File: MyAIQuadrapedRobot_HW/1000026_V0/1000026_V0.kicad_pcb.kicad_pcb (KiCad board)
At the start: 4 copper layers, 100 x 70 mm, 27 parts, among them J1 533750410, J2 0525591853, J3 532580229, J5 532580229, J9 0525591853, SW1 TL3305CF260QG, U1 TXB0108PWR, U2 MAX7480ESA+

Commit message: Start of version V0b.
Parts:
- moved D1 0.11 mm to (158.5, 115.8), turned to -90 degrees
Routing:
- net 7.4V: track 211.3 -> 195.4 mm
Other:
- board text added: "+7.4V IN"
- board text removed: "+7.5V IN"
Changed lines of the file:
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@@
   )
   (footprint "myKiCadGlobalFootprintLibrary:1N4148WT" (layer "F.Cu")
-    (at 158.5398 115.6882 90)
+    (at 158.4898 115.7882 -90)
     (tags "1N4148WX-TP ")
     (property "Sheetfile" "1000026_V0.kicad_pcb.kicad_sch")
     (property "Sheetname" "")
     (attr smd)
-    (fp_text reference "D1" (at -0.05 1.775 90 unlocked) (layer "F.SilkS")
-      (effects (font (size 0.75 0.75) (thickness 0.12)))
-    )
-    (fp_text value "1N4148WX-TP" (at 0 3.0734 90 unlocked) (layer "F.Fab") hide
-      (effects (font (size 0.75 0.75) (thickness 0.12)))
-    )
-    (fp_text user "+" (at 1.375 -1.975 90 unlocked) (layer "F.SilkS")
+    (fp_text reference "D1" (at -0.125 1.7 90 unlocked) (layer "F.SilkS")
+      (effects (font (size 0.75 0.75) (thickness 0.12)))
+    )
+    (fp_text value "1N4148WX-TP" (at 0 3.0734 -90 unlocked) (layer "F.Fab") hide
+      (effects (font (size 0.75 0.75) (thickness 0.12)))
+    )
+    (fp_text user "+" (at 1.375 -1.975 -90 unlocked) (layer "F.SilkS")
       (effects (font (size 0.75 0.75) (thickness 0.12)))
     )
@@
       (effects (font (size 0.75 0.75) (thickness 0.12)))
     )
-    (fp_text user "-" (at -1.6 -2 90 unlocked) (layer "F.SilkS")
-      (effects (font (size 0.75 0.75) (thickness 0.12)))
-    )
-    (fp_text user "${REFERENCE}" (at 3.7084 -1.905 90 unlocked) (layer "F.Fab") hide
-      (effects (font (size 0.75 0.75) (thickness 0.12)))
-    )
-    (fp_text user "*" (at -4.4958 -0.8128 90 unlocked) (layer "F.Fab") hide
+    (fp_text user "-" (at -1.6 -2 -90 unlocked) (layer "F.SilkS")
+      (effects (font (size 0.75 0.75) (thickness 0.12)))
+    )
+    (fp_text user "${REFERENCE}" (at 3.7084 -1.905 -90 unlocked) (layer "F.Fab") hide
+      (effects (font (size 0.75 0.75) (thickness 0.12)))
+    )
+    (fp_text user "*" (at -4.4958 -0.8128 -90 unlocked) (layer "F.Fab") hide
       (effects (font (size 0.75 0.75) (thickness 0.12)))
     )
@@
     (fp_line (start -0.9017 -0.33655) (end -0.56515 -0.6731) (layer "F.Fab") (width 0.0254))
     (fp_line (start -0.508 -1.9304) (end 0.254 -1.4224) (layer "F.Fab") (width 0.0254))
-    (pad "1" smd rect (at -1.1303 0 90) (size 1.157199 0.4664) (layers "F.Cu" "F.Paste" "F.Mask")
+    (pad "1" smd rect (at -1.1303 0 270) (size 1.157199 0.4664) (layers "F.Cu" "F.Paste" "F.Mask")
       (net 73 "7.4V") (pintype "unspecified"))
-    (pad "2" smd rect (at 1.1303 0 90) (size 1.157199 0.4664) (layers "F.Cu" "F.Paste" "F.Mask")
+    (pad "2" smd rect (at 1.1303 0 270) (size 1.157199 0.4664) (layers "F.Cu" "F.Paste" "F.Mask")
       (net 73 "7.4V") (pintype "unspecified"))
     (model "${MY_KICAD_SYMBOL_DIR}/3Dmodels/1N4148WT.STEP"
@@
     (effects (font (size 0.75 0.75) (thickness 0.12)))
   )
-  (gr_text "+7.5V IN" (at 109.2898 121.1382) (layer "F.SilkS")
+  (gr_text "+7.4V IN" (at 109.2898 121.1382) (layer "F.SilkS")
     (effects (font (size 0.75 0.75) (thickness 0.12)))
   )
@@
     (effects (font (size 0.75 0.75) (thickness 0.12)))
   )
-  (dimension (type orthogonal) (layer "F.Mask")
-    (pts (xy 187.3898 53.1632) (xy 187.2148 123.2882))
-    (height 21.15)
+  (dimension (type orthogonal) (layer "User.2")
+    (pts (xy 192.4648 53.2132) (xy 193.6398 123.2132))
+    (height 19.825)
     (orientation 1)
-    (gr_text "70.1250 mm" (at 207.3898 88.2257 90) (layer "F.Mask")
+    (gr_text "70.0000 mm" (at 211.1398 88.2132 90) (layer "User.2")
+      (effects (font (size 1 1) (thickness 0.15)))
+    )
+    (format (units 3) (units_format 1) (precision 4))
+    (style (thickness 0.15) (arrow_length 1.27) (text_position_mode 0) (extension_height 0.58642) (extension_offset 0.5) keep_text_aligned)
+  )
+  (dimension (type orthogonal) (layer "User.2")
+    (pts (xy 193.0228 57.2132) (xy 193.5308 119.2132))
+    (height 13.208)
+    (orientation 1)
+    (gr_text "62.0000 mm" (at 205.0808 88.2132 90) (layer "User.2")
+      (effects (font (size 1 1) (thickness 0.15)))
+    )
+    (format (units 3) (units_format 1) (precision 4))
+    (style (thickness 0.15) (arrow_length 1.27) (text_position_mode 0) (extension_height 0.58642) (extension_offset 0.5) keep_text_aligned)
+  )
+  (dimension (type orthogonal) (layer "User.2")
+    (pts (xy 101.2398 57.2132) (xy 193.2398 57.2132))
+    (height -11.366)
+    (orientation 0)
+    (gr_text "92.0000 mm" (at 147.2398 44.6972) (layer "User.2")
+      (effects (font (size 1 1) (thickness 0.15)))
+    )
+    (format (units 3) (units_format 1) (precision 4))
+    (style (thickness 0.15) (arrow_length 1.27) (text_position_mode 0) (extension_height 0.58642) (extension_offset 0.5) keep_text_aligned)
+  )
+  (dimension (type orthogonal) (layer "User.2")
+    (pts (xy 97.2398 57.9882) (xy 197.2398 58.6132))
+    (height -14.7)
+    (orientation 0)
+    (gr_text "100.0000 mm" (at 147.2398 42.1382) (layer "User.2")
       (effects (font (size 1 1) (thickness 0.15)))
     )
@@
   (segment (start 101.2302 95.0578) (end 99.9398 93.7674) (width 0.25) (layer "B.Cu") (net 72))
   (segment (start 99.9398 93.7674) (end 99.9398 74.0132) (width 0.25) (layer "B.Cu") (net 72))
-  (segment (start 158.5398 112.6132) (end 158.5398 114.5579) (width 0.25) (layer "F.Cu") (net 73))
+  (segment (start 158.4898 114.6579) (end 158.4898 112.6632) (width 0.25) (layer "F.Cu") (net 73))
   (segment (start 184.3001 72.7312) (end 189.3468 72.7312) (width 0.25) (layer "F.Cu") (net 73))
   (segment (start 143.7498 118.0932) (end 143.7498 119.5532) (width 0.25) (layer "F.Cu") (net 73))
-  (segment (start 158.5398 116.8185) (end 158.5398 118.5632) (width 0.25) (layer "F.Cu") (net 73))
+  (segment (start 158.4898 118.5132) (end 158.5398 118.5632) (width 0.25) (layer "F.Cu") (net 73))
+  (segment (start 158.4898 112.6632) (end 158.5398 112.6132) (width 0.25) (layer "F.Cu") (net 73))
+  (segment (start 158.4898 116.9185) (end 158.4898 118.5132) (width 0.25) (layer "F.Cu") (net 73))
   (via (at 158.5398 112.6132) (size 0.8) (drill 0.4) (layers "F.Cu" "B.Cu") (net 73))
   (via (at 189.3468 72.7312) (size 0.8) (drill 0.4) (layers "F.Cu" "B.Cu") (net 73))
@@
   (segment (start 158.5398 111.3132) (end 158.5398 112.6132) (width 0.25) (layer "In1.Cu") (net 73))
   (segment (start 160.6398 113.6132) (end 159.6398 112.6132) (width 0.25) (layer "In1.Cu") (net 73))
-  (segment (start 122.6678 118.8132) (end 138.6648 118.8132) (width 0.25) (layer "In1.Cu") (net 73))
   (segment (start 122.6678 119.7212) (end 121.1438 121.2452) (width 0.25) (layer "In1.Cu") (net 73))
   (segment (start 138.0358 115.6572) (end 138.0358 118.1842) (width 0.25) (layer "In1.Cu") (net 73))

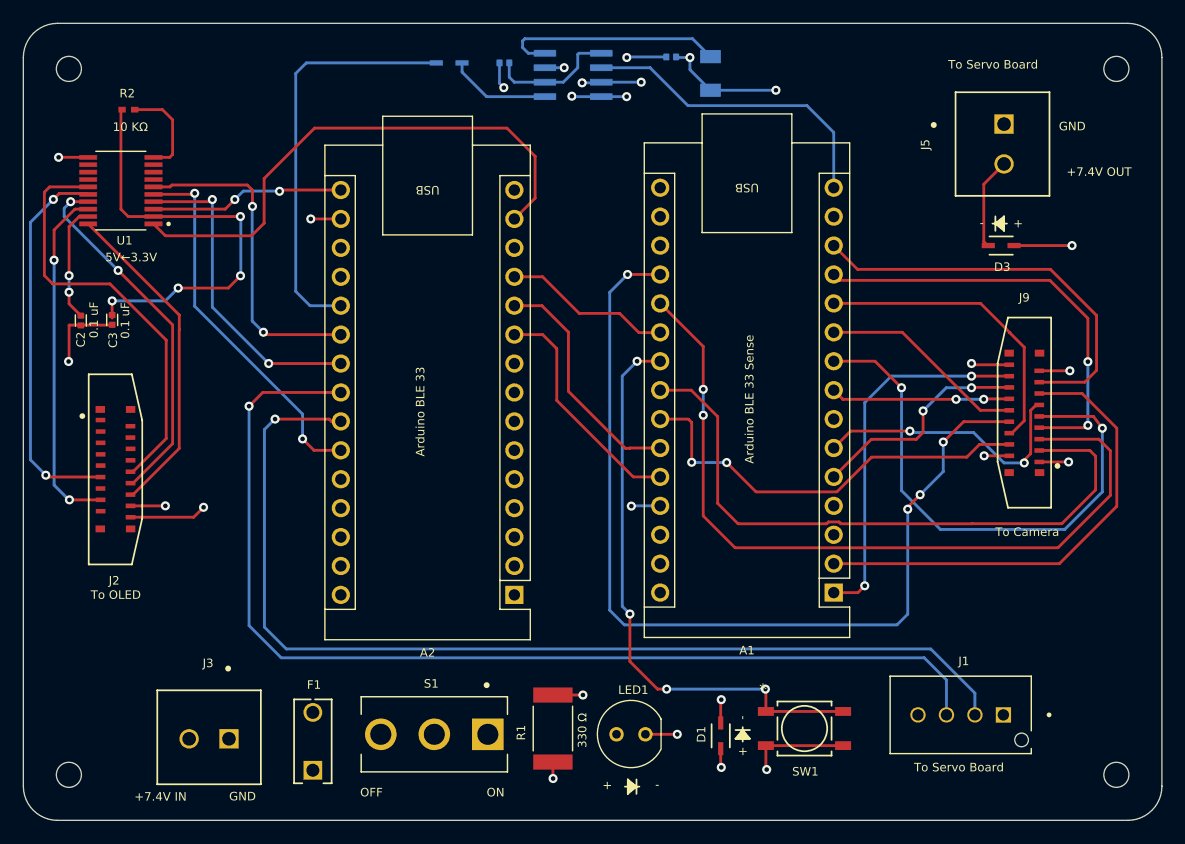
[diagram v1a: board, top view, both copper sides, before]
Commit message: Revisions in progress for change in sizes of some SMD components.
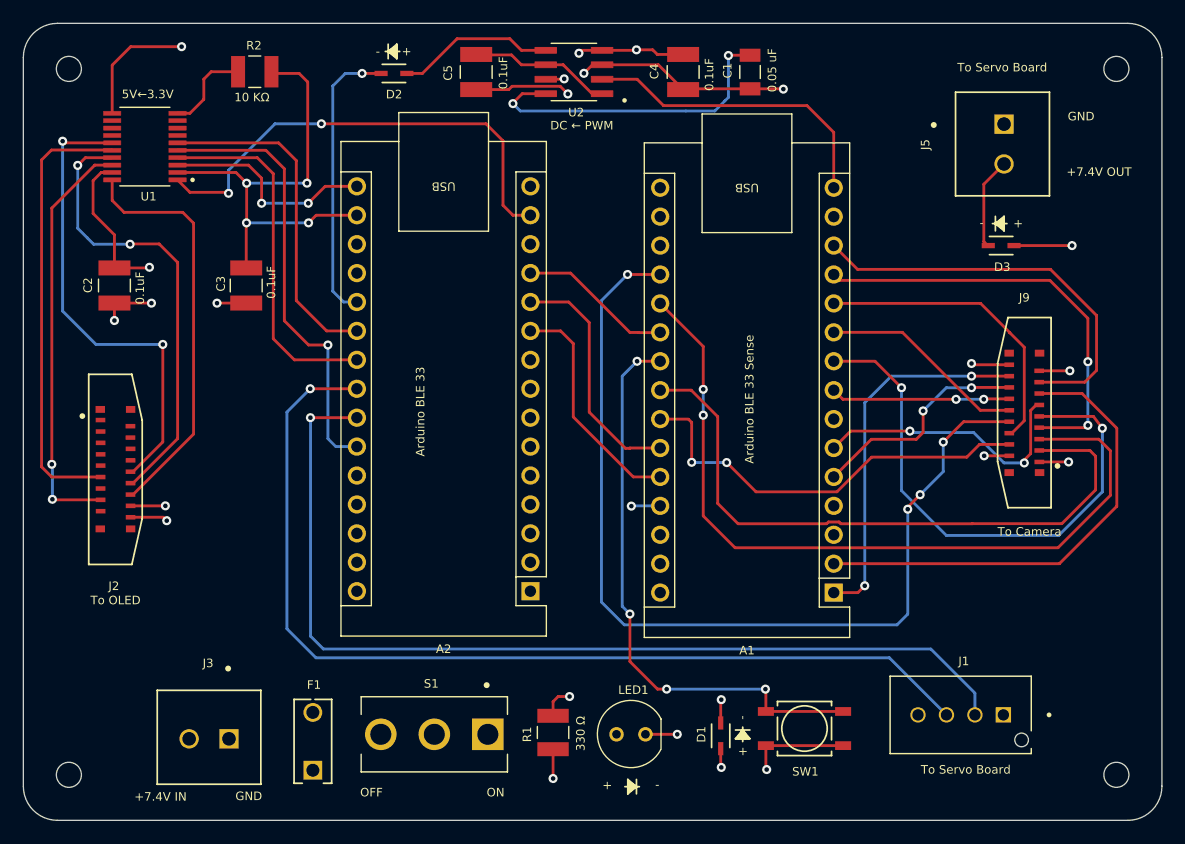
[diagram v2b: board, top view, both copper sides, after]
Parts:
- C1, D2, U2: moved to F.Cu
- C2, C3: value CL05A104KA5NNNC -> 12102C104KAT2A; footprint myKiCadGlobalFootprintLibrary:CAPC1005X55N -> myKiCadGlobalFootprintLibrary:12102C104KAT2A
- C4, C5: value CL05A104KA5NNNC -> 12102C104KAT2A; footprint myKiCadGlobalFootprintLibrary:CAPC1005X55N -> myKiCadGlobalFootprintLibrary:12102C104KAT2A; moved to F.Cu
- R1: value RMCF2512FT330R -> RMCF1210JT330R; footprint myKiCadGlobalFootprintLibrary:RESC6332X70N -> myKiCadGlobalFootprintLibrary:RMCF1210JT330R
- R2: value RC0402JR-0710KL -> RMCF1210JT10K0; footprint myKiCadGlobalFootprintLibrary:RC0402JR-0710KL -> myKiCadGlobalFootprintLibrary:RMCF1210JT10K0
- moved C3 12.2 mm to (116.8, 76.2)
- moved R2 11.6 mm to (117.6, 57.5), turned to 180 degrees
- moved D2 4.94 mm to (129.8, 57.6)
- moved U1 4.40 mm to (107.9, 64.0)
- moved C2 4.26 mm to (105.2, 76.2)
- moved C1 3.48 mm to (161.1, 57.5), turned to -90 degrees
- moved C5 2.60 mm to (137.0, 57.5), turned to -90 degrees
- moved C4 1.69 mm to (155.2, 57.5), turned to -90 degrees
- moved A2 1.45 mm to (141.8, 103.1)
- moved R1 0.35 mm to (143.8, 115.5)
- moved U2 0.27 mm to (145.6, 57.5)
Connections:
- C1 pad 1: GND -> /CLK
- C1 pad 2: /CLK -> GND
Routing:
- net GND: track 376.5 -> 405.4 mm
- net Analog: track 36.4 -> 25.2 mm, vias 0 -> 1
- net 5V_2: track 57.8 -> 68.7 mm, vias 3 -> 2
- net /CLK: track 20.0 -> 28.5 mm, vias 0 -> 2
- net DC_5V: track 32.1 -> 40.1 mm
- net MOSI_5V: track 29.0 -> 36.0 mm
- net SDA_2: track 94.1 -> 87.1 mm
- net RST: track 32.9 -> 39.2 mm, vias 2 -> 1
- net SCK_5V: track 30.7 -> 36.7 mm
- net 3.3V_2: track 47.3 -> 41.7 mm, vias 5 -> 4
- net SDL_2: track 91.2 -> 85.6 mm
- net /MOSI: track 47.5 -> 41.8 mm, vias 0 -> 2
- net RST_5V: track 33.8 -> 39.1 mm, vias 2 -> 0
- net 7.4V: track 195.4 -> 190.3 mm
- net /DC_out: track 8.98 -> 13.9 mm
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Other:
- board text added: "1000026_V0b Copyright © James Canova, August 2023, Victoria, BC Canada"
- board text added: "DC ← PWM"
- board text removed: "1000026_V0a Copyright © James Canova, June 2023, Victoria, BC Canada"
- board text removed: "PWM → DC (low pass filter)"

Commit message: Minor revisions.
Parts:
- C1: value 12065C503JAT2A -> CAPC3216X94N
- C2, C3, C4, C5: value 12102C104KAT2A -> CAPC3325X127N
- J1: value 533750410 -> MOLEX_533750410
- LED1: value C503B-GAN-CB0F0791 -> C503B
- R1: value RMCF1210JT330R -> RESC3225X70N
- R2: value RMCF1210JT10K0 -> RESC3225X70N
- S1: value 500SSP1S2M2QEA -> Slider_switch_500SSP1S2M2QEA
- SW1: value TL3305CF260QG -> SW4_TL3305CF260QG_EWI
- moved D3 3.85 mm to (186.6, 71.1)
- moved J5 2.46 mm to (180.9, 62.0), turned to 180 degrees
- moved C1 2.08 mm to (163.1, 57.4)
- moved U2 1.87 mm to (147.5, 57.6)
- moved C4 1.30 mm to (156.5, 57.5)
- moved R2 0.29 mm to (117.3, 57.6)
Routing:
- net GND: track 405.4 -> 416.2 mm
- net /CLK: track 28.5 -> 23.6 mm
- net 7.4V: track 190.3 -> 185.4 mm
- net 3.3V_1: track 100.8 -> 98.4 mm
- net /COM: track 12.5 -> 14.5 mm
- net PWM: track 27.1 -> 25.2 mm
- net /DC_out: track 13.9 -> 15.8 mm
- net Net-(D3-Pad1): track 8.05 -> 9.54 mm
- net D2: track 41.9 -> 43.2 mm
- net D3: track 19.8 -> 20.5 mm
- net OE: track 7.87 -> 7.23 mm
- net D6: track 48.5 -> 49.1 mm

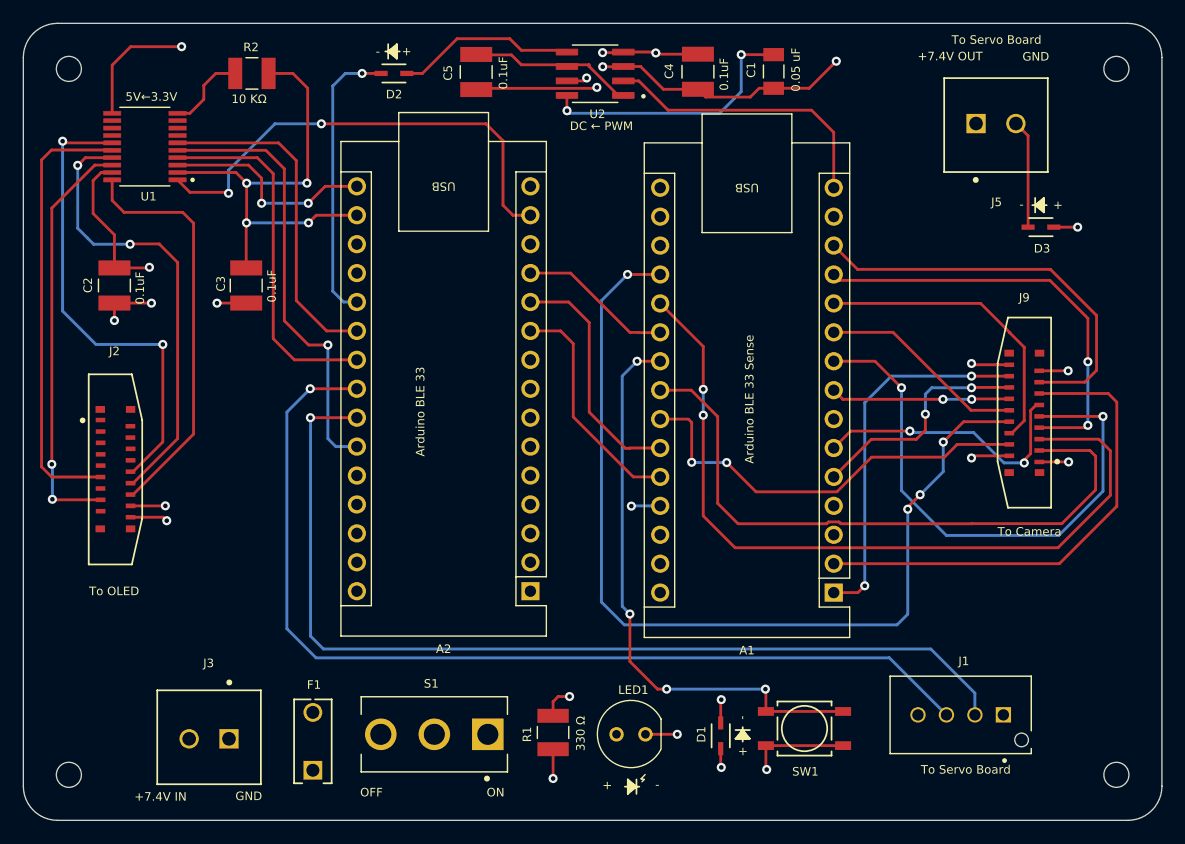
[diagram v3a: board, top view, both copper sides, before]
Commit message: Moved LED to clear post.
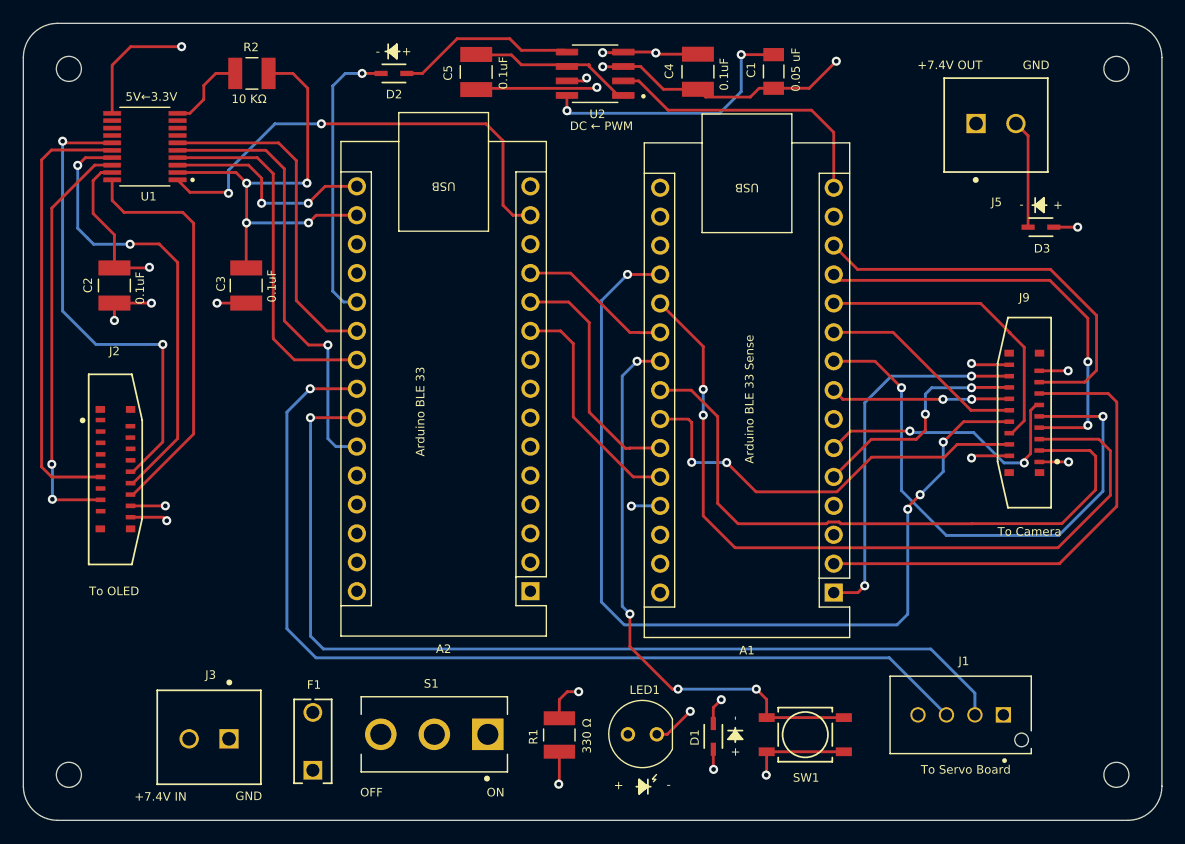
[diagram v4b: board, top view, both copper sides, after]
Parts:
- C1: value CAPC3216X94N -> 12065C503JAT2A
- C2, C3, C4, C5: value CAPC3325X127N -> 12102C104KAT2A
- J1: value MOLEX_533750410 -> 533750410
- LED1: value C503B -> C503B-GAN-CB0F0791
- R1: value RESC3225X70N -> RMCF1210JT330R
- R2: value RESC3225X70N -> RMCF1210JT10K0
- S1: value Slider_switch_500SSP1S2M2QEA -> 500SSP1S2M2QEA
- SW1: value SW4_TL3305CF260QG_EWI -> TL3305CF260QG
- moved LED1 1.00 mm to (152.9, 115.7)
- moved D1 0.65 mm to (157.8, 115.8)
- moved R1 0.59 mm to (144.3, 115.7)
- moved SW1 0.54 mm to (165.9, 115.7)
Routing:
- net 7.4V: track 185.4 -> 182.3 mm
- net Net-(LED1-Pad2): track 8.78 -> 10.7 mm
- net GND: track 416.2 -> 417.3 mm
- net PB: track 50.9 -> 50.2 mm

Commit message: Added components for 5V regulator.
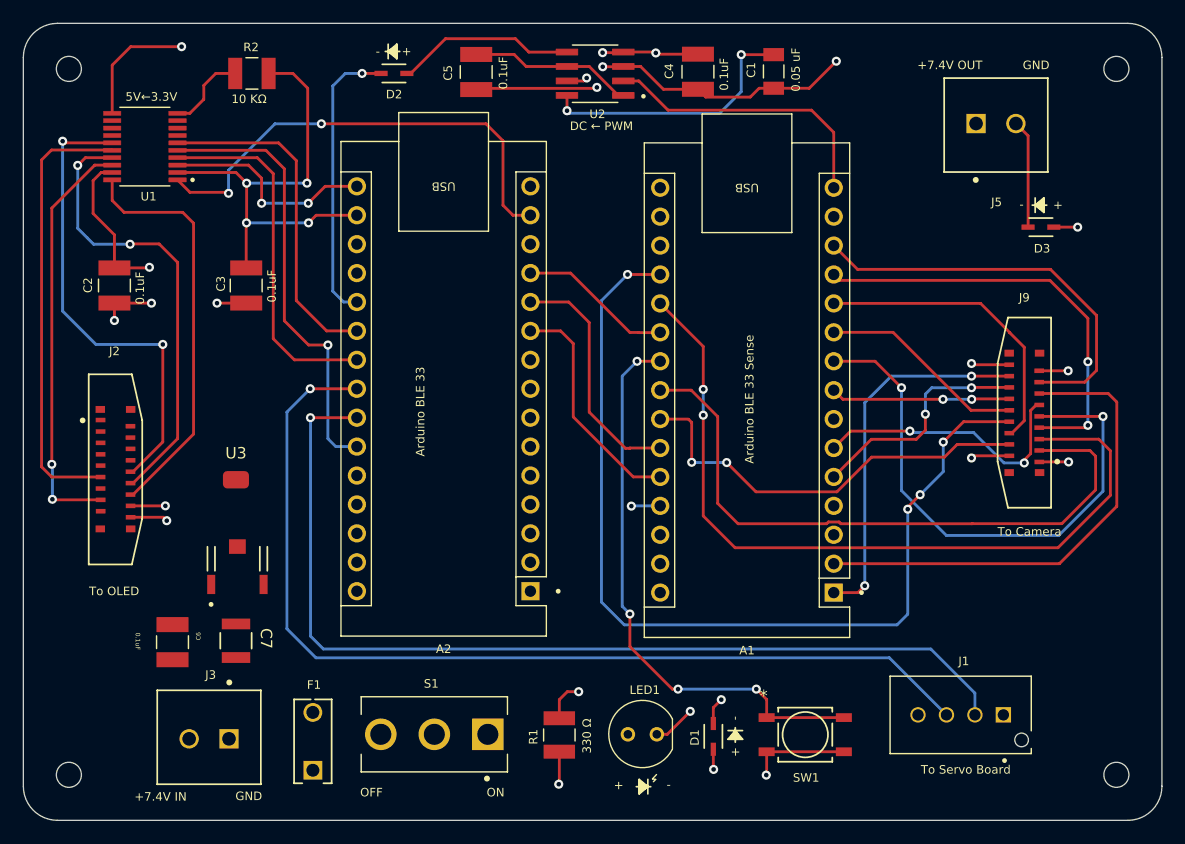
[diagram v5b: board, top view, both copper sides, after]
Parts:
- added C6: 12102C104KAT2A, myKiCadGlobalFootprintLibrary:12102C104KAT2A, F.Cu at (110.3, 107.6)
- added C7: CL32A106KAULNNE, myKiCadGlobalFootprintLibrary:CL32A106KAULNNE, F.Cu at (115.9, 107.4)
- added U3: BD450M5FP-CE2, myKiCadGlobalFootprintLibrary:BD450M5FP-CE2, F.Cu at (116.0, 95.7)
